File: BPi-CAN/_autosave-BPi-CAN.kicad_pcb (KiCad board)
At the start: 2 copper layers, 100 x 100 mm, 102 parts, among them J1 RJ45, J2 RJ45, J3 RJ45, J4 RJ45, P1 BPi, P10 SPI, P11 SNIFFER, P12 CAN-Bus, P13 USB, P14 CAN-Bus, P15 POWER, P16 CAN, P17 CAN, P18 CAN, P19 TERM, P2 S88, P20 S88 CONN, P21 RS232 Con, P22 S88, P3 CONN_02X04, P4 CONN_01X02, P5 TERM, P6 S88, P7 I2C-Bus, P8 RS485, P9 RS232, U1 MCP2562, U10 MCP2562, U11 6N137, U12 ISO1050, U13 FT230XS, U2 LM7805, U3 6N137, U4 6N137, U5 6N137, U6 6N137, U7 ADuM1251BR, U8 MAX3072E, U9 MAX3232

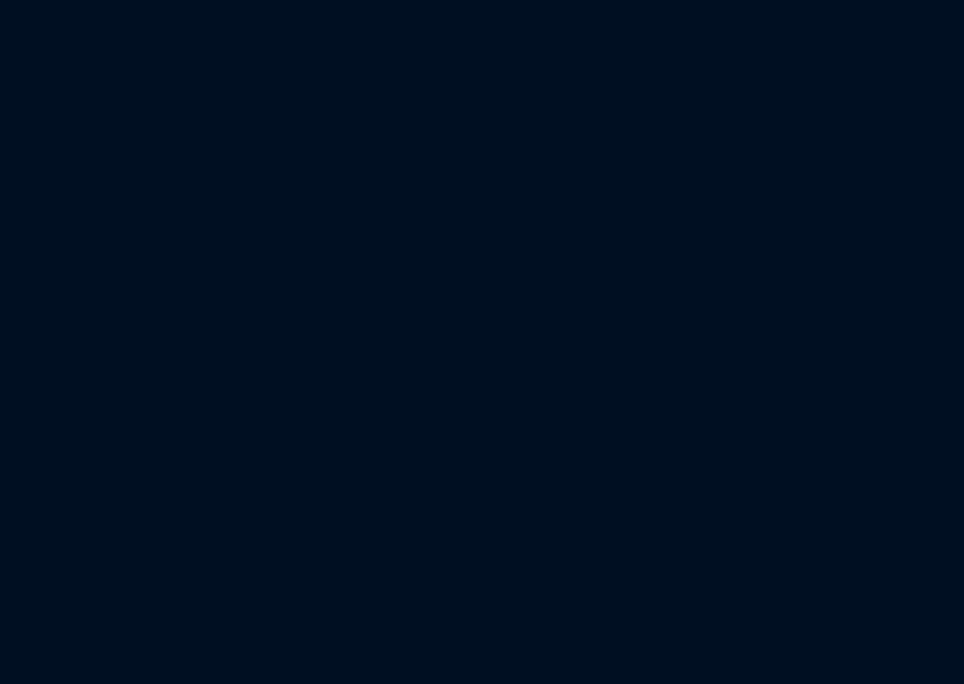
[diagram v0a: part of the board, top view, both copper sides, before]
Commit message: add DCDC converter
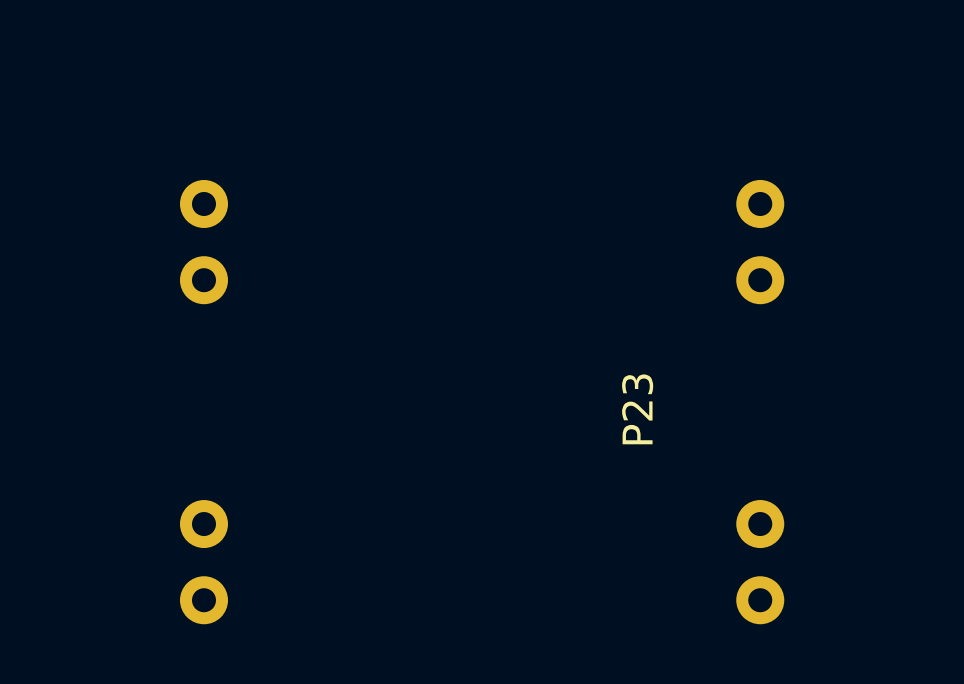
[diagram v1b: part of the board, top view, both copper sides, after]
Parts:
- added P23: CONN_01X08, 78xx:DCDC, F.Cu at (130.9, 162.7)
- P4: value CONN_01X02 -> BPi Con
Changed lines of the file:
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@@
 (kicad_pcb (version 4) (host pcbnew 4.0.1-3.201512221402+6198~38~ubuntu14.04.1-stable)
   (general
-    (links 245)
-    (no_connects 145)
+    (links 253)
+    (no_connects 153)
     (area 99.924999 39.924999 200.075001 140.075001)
     (thickness 1.6)
-    (drawings 80)
+    (drawings 82)
     (tracks 513)
     (zones 0)
-    (modules 102)
+    (modules 103)
     (nets 127)
   )
@@
       (effects (font (size 1 1) (thickness 0.15)) (justify mirror))
     )
-    (fp_text value CONN_01X02 (at 0 3.1) (layer B.Fab)
+    (fp_text value "BPi Con" (at 0 3.1) (layer B.Fab)
       (effects (font (size 1 1) (thickness 0.15)) (justify mirror))
     )
@@
     )
   )
+  (module 78xx:DCDC (layer F.Cu)
+    (at 130.937 162.687 270)
+    (descr "DC-DC Board")
+    (tags DCDC)
+    (fp_text reference P23 (at 0.254 -5.22 270) (layer F.SilkS)
+      (effects (font (size 1 1) (thickness 0.15)))
+    )
+    (fp_text value CONN_01X08 (at -3.683 -7.53 270) (layer F.Fab)
+      (effects (font (size 1 1) (thickness 0.15)))
+    )
+    (fp_line (start -8.382 -11.049) (end -8.382 11.049) (layer F.CrtYd) (width 0.0508))
+    (fp_line (start 8.382 -11.049) (end 8.382 11.049) (layer F.CrtYd) (width 0.0508))
+    (fp_line (start -8.382 -11.049) (end 8.382 -11.049) (layer F.CrtYd) (width 0.0508))
+    (fp_line (start -8.382 11.049) (end 8.382 11.049) (layer F.CrtYd) (width 0.0508))
+    (pad 1 thru_hole oval (at -6.604 -9.271 270) (size 1.6 1.6) (drill 0.8) (layers *.Cu *.Mask F.SilkS)
+      (net 60 /CVCC))
+    (pad 2 thru_hole oval (at -4.064 -9.271 270) (size 1.6 1.6) (drill 0.8) (layers *.Cu *.Mask F.SilkS)
+      (net 60 /CVCC))
+    (pad 3 thru_hole oval (at 4.064 -9.271 270) (size 1.6 1.6) (drill 0.8) (layers *.Cu *.Mask F.SilkS)
+      (net 55 /CB4))
+    (pad 4 thru_hole oval (at 6.604 -9.271 270) (size 1.6 1.6) (drill 0.8) (layers *.Cu *.Mask F.SilkS)
+      (net 55 /CB4))
+    (pad 5 thru_hole oval (at -6.604 9.271 270) (size 1.6 1.6) (drill 0.8) (layers *.Cu *.Mask F.SilkS)
+      (net 57 /CB6))
+    (pad 6 thru_hole oval (at -4.064 9.271 270) (size 1.6 1.6) (drill 0.8) (layers *.Cu *.Mask F.SilkS)
+      (net 57 /CB6))
+    (pad 7 thru_hole oval (at 4.064 9.271 270) (size 1.6 1.6) (drill 0.8) (layers *.Cu *.Mask F.SilkS)
+      (net 55 /CB4))
+    (pad 8 thru_hole oval (at 6.604 9.271 270) (size 1.6 1.6) (drill 0.8) (layers *.Cu *.Mask F.SilkS)
+      (net 55 /CB4))
+  )
+  (dimension 16.637 (width 0.3) (layer Dwgs.User)
+    (gr_text "0.6550 in" (at 145.495 162.7505 90) (layer Dwgs.User)
+      (effects (font (size 1.5 1.5) (thickness 0.3)))
+    )
+    (feature1 (pts (xy 141.732 154.432) (xy 146.845 154.432)))
+    (feature2 (pts (xy 141.732 171.069) (xy 146.845 171.069)))
+    (crossbar (pts (xy 144.145 171.069) (xy 144.145 154.432)))
+    (arrow1a (pts (xy 144.145 154.432) (xy 144.731421 155.558504)))
+    (arrow1b (pts (xy 144.145 154.432) (xy 143.558579 155.558504)))
+    (arrow2a (pts (xy 144.145 171.069) (xy 144.731421 169.942496)))
+    (arrow2b (pts (xy 144.145 171.069) (xy 143.558579 169.942496)))
+  )
+  (dimension 22.098 (width 0.3) (layer Dwgs.User)
+    (gr_text "0.8700 in" (at 130.937 174.197) (layer Dwgs.User)
+      (effects (font (size 1.5 1.5) (thickness 0.3)))
+    )
+    (feature1 (pts (xy 141.986 170.815) (xy 141.986 175.547)))
+    (feature2 (pts (xy 119.888 170.815) (xy 119.888 175.547)))
+    (crossbar (pts (xy 119.888 172.847) (xy 141.986 172.847)))
+    (arrow1a (pts (xy 141.986 172.847) (xy 140.859496 173.433421)))
+    (arrow1b (pts (xy 141.986 172.847) (xy 140.859496 172.260579)))
+    (arrow2a (pts (xy 119.888 172.847) (xy 121.014504 173.433421)))
+    (arrow2b (pts (xy 119.888 172.847) (xy 121.014504 172.260579)))
+  )
   (gr_text GND (at 139.4714 50.6222) (layer F.SilkS)
